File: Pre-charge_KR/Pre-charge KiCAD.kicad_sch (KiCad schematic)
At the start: 51 parts, among them IC2 TLV1701AIDBVT, IC3 SN74LVC1G11DCKRE4, IC4 SN74LVC1G08IDCKRQ1, J1 Conn_01x02, J2 Conn_01x06, J3 Conn_01x02, J4 Conn_01x02, K2 G5Q-1A4-DC12, K3 67-1-A-12/2D, Q2 2N7000, Q4 2N7000, U1 HCPL-817-000E, U13 HCPL-817-000E, U2 MCP1703AT-3302E/MBVAO, U8 SN74LVC1G04QDBVRQ1

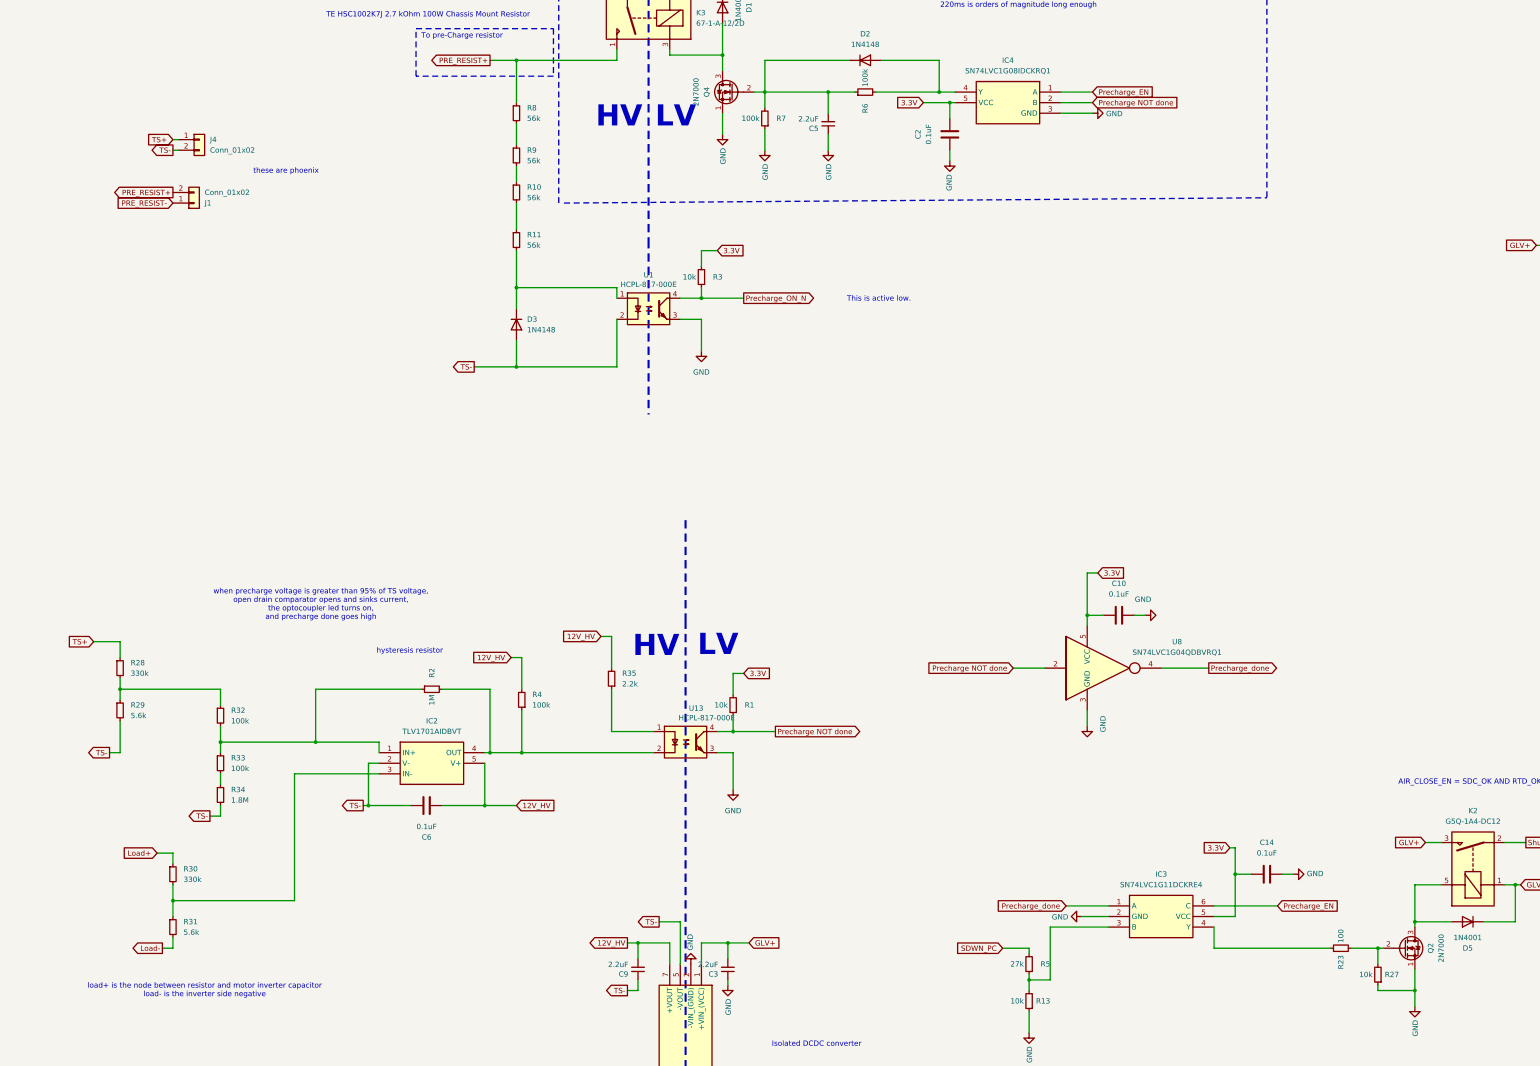
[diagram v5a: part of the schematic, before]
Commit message: slave with new fuses added
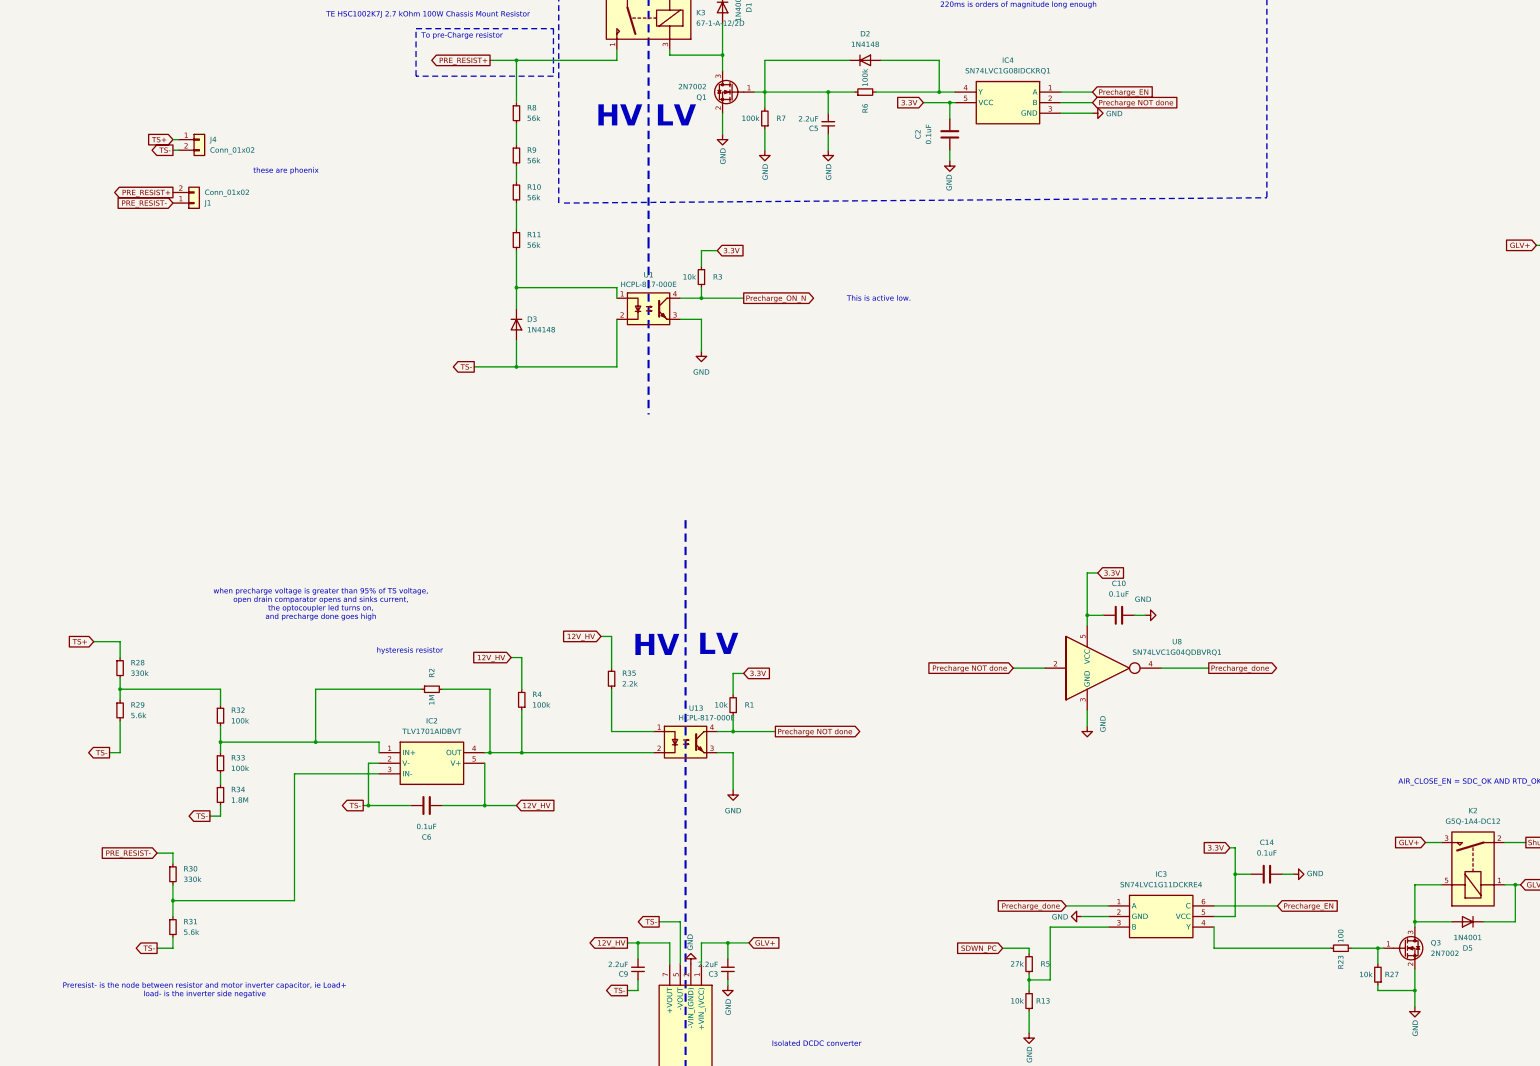
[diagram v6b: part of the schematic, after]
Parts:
- removed Q2, Q4: 2N7000, Package_TO_SOT_THT:TO-92_Inline, symbol Transistor_FET:2N7000
- added Q1, Q3: 2N7002, Package_TO_SOT_SMD:SOT-23, symbol Transistor_FET:2N7002
- R4: Part Number MCF 0.25W 100k -> MCF 0.25W 100K
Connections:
- net Load+ is gone; now on net PRE_RESIST-: R30.1
- net Load- is gone; now on net TS-: R31.2
- net GND: now also Q1.2 (S), Q3.2 (S)
- net at R23.2, R27.2: now also Q3.1 (G)
- net at C5.2, D2.1 (K), R6.1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: now also Q1.1 (G)
- net at D5.2 (A), K2.5: now also Q3.3 (D)
- net at D1.2 (A), K3.3: now also Q1.3 (D)
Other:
- note added: "Preresist- is the node between resistor and motor inverter capacitor, ie Load+ load- is the inverter side negative"
- note removed: "load+ is the node between resistor and motor inverter capacitor load- is the inverter side negative"

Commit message: master and slave updated
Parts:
- J3: Part Number B6B-XH-A -> B2B-XH-A
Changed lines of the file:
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@@
 			)
 		)
-		(property "Part Number" "B6B-XH-A"
+		(property "Part Number" "B2B-XH-A"
 			(at 434.34 203.2 0)
 			(effects
